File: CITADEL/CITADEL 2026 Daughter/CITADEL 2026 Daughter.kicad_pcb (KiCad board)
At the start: 2 copper layers, 35.8 x 35.5 mm, 4 parts, among them J1 Servo_Daughter

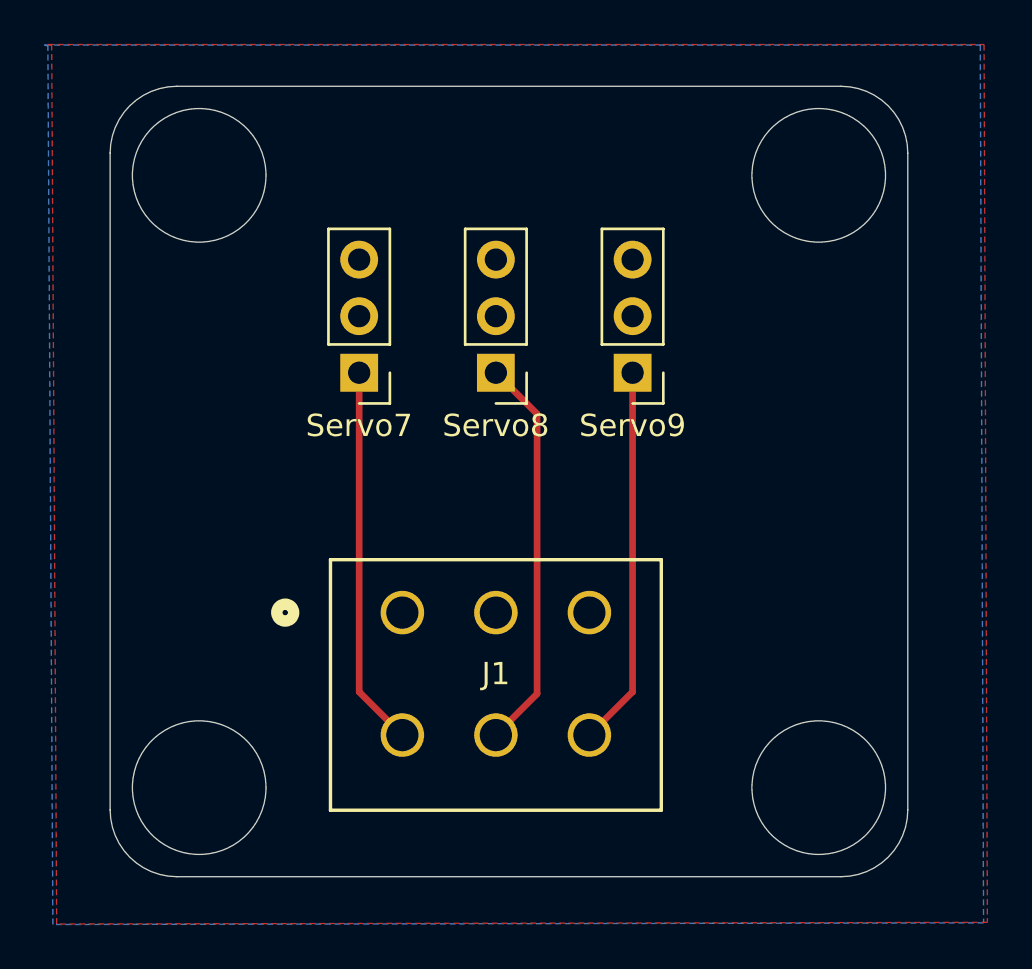
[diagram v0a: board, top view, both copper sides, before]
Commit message: Changed board to be square
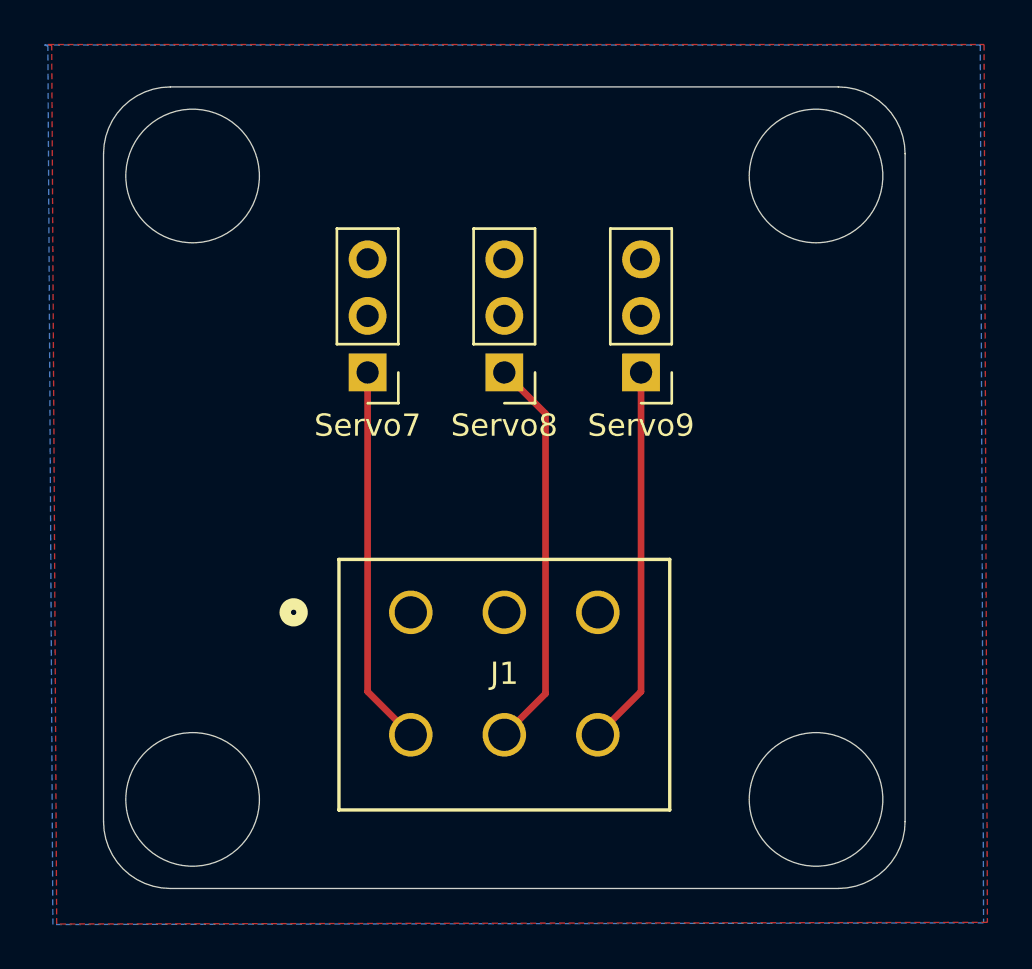
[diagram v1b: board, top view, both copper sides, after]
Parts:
- moved J1 0.38 mm to (39.1, 45.3)
- moved Servo7 0.38 mm to (37.1, 34.5)
- moved Servo8 0.38 mm to (43.3, 34.5)
- moved Servo9 0.38 mm to (49.4, 34.5)
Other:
- board size 35.8 x 35.5 mm -> 36 x 36 mm
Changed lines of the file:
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@@
 	(footprint "Connector_PinHeader_2.54mm:PinHeader_1x03_P2.54mm_Vertical"
 		(layer "F.Cu")
-		(at 36.76 34.49 180)
+		(at 37.13868 34.47748 180)
 		(descr "Through hole straight pin header, 1x03, 2.54mm pitch, single row")
 		(tags "Through hole pin header THT 1x03 2.54mm single row")
@@
 	(footprint "Jayse_Footprints:CONN_SD-5566-002_06_MOL"
 		(layer "F.Cu")
-		(at 38.700001 45.264001)
+		(at 39.078681 45.251481)
 		(tags "39281063 ")
 		(property "Reference" "J1"
@@
 	(footprint "Connector_PinHeader_2.54mm:PinHeader_1x03_P2.54mm_Vertical"
 		(layer "F.Cu")
-		(at 49.04 34.49 180)
+		(at 49.41868 34.47748 180)
 		(descr "Through hole straight pin header, 1x03, 2.54mm pitch, single row")
 		(tags "Through hole pin header THT 1x03 2.54mm single row")
@@
 	(footprint "Connector_PinHeader_2.54mm:PinHeader_1x03_P2.54mm_Vertical"
 		(layer "F.Cu")
-		(at 42.9 34.49 180)
+		(at 43.27868 34.47748 180)
 		(descr "Through hole straight pin header, 1x03, 2.54mm pitch, single row")
 		(tags "Through hole pin header THT 1x03 2.54mm single row")
@@
 	)
 	(gr_circle
-		(center 57.4 25.625)
-		(end 60.4 25.625)
+		(center 57.27868 25.65368)
+		(end 60.27868 25.65368)
 		(stroke
 			(width 0.05)
@@
 		(layer "Edge.Cuts")
 	)
+	(gr_arc
+		(start 28.27868 57.65368)
+		(mid 26.15736 56.775)
+		(end 25.27868 54.65368)
+		(stroke
+			(width 0.05)
+			(type default)
+		)
+		(layer "Edge.Cuts")
+	)
 	(gr_circle
-		(center 57.4 53.125)
-		(end 60.4 53.125)
+		(center 57.27868 53.65368)
+		(end 60.27868 53.65368)
 		(stroke
 			(width 0.05)
@@
 	)
 	(gr_arc
-		(start 58.4 21.625)
-		(mid 60.52132 22.50368)
-		(end 61.4 24.625)
+		(start 61.27868 54.65368)
+		(mid 60.4 56.775)
+		(end 58.27868 57.65368)
 		(stroke
 			(width 0.05)
@@
 		(layer "Edge.Cuts")
 	)
-	(gr_line
-		(start 58.4 57.125)
-		(end 28.575 57.125)
+	(gr_arc
+		(start 25.27868 24.65368)
+		(mid 26.15736 22.53236)
+		(end 28.27868 21.65368)
 		(stroke
 			(width 0.05)
@@
 	)
 	(gr_circle
-		(center 29.575 53.125)
-		(end 32.575 53.125)
+		(center 29.27868 53.65368)
+		(end 32.27868 53.65368)
 		(stroke
 			(width 0.05)
@@
 		(layer "Edge.Cuts")
 	)
-	(gr_arc
-		(start 28.575 57.125)
-		(mid 26.45368 56.24632)
-		(end 25.575 54.125)
+	(gr_line
+		(start 28.27868 21.65368)
+		(end 58.27868 21.65368)
 		(stroke
 			(width 0.05)
@@
 		(layer "Edge.Cuts")
 	)
-	(gr_arc
-		(start 61.4 54.125)
-		(mid 60.52132 56.24632)
-		(end 58.4 57.125)
+	(gr_line
+		(start 61.27868 24.65368)
+		(end 61.27868 54.65368)
 		(stroke
 			(width 0.05)
@@
 	)
 	(gr_circle
-		(center 29.575 25.625)
-		(end 32.575 25.625)
+		(center 29.27868 25.65368)
+		(end 32.27868 25.65368)
 		(stroke
 			(width 0.05)
@@
 	)
 	(gr_line
-		(start 25.575 54.125)
-		(end 25.575 24.625)
+		(start 58.27868 57.65368)
+		(end 28.27868 57.65368)
 		(stroke
 			(width 0.05)
@@
 	)
 	(gr_arc
-		(start 25.575 24.625)
-		(mid 26.45368 22.50368)
-		(end 28.575 21.625)
+		(start 58.27868 21.65368)
+		(mid 60.4 22.53236)
+		(end 61.27868 24.65368)
 		(stroke
 			(width 0.05)
@@
 	)
 	(gr_line
-		(start 61.4 24.625)
-		(end 61.4 54.125)
+		(start 25.27868 54.65368)
+		(end 25.27868 24.65368)
 		(stroke
 			(width 0.05)
@@
 		(layer "Edge.Cuts")
 	)
-	(gr_line
-		(start 28.575 21.625)
-		(end 58.4 21.625)
-		(stroke
-			(width 0.05)
-			(type default)
-		)
-		(layer "Edge.Cuts")
+	(dimension
+		(type orthogonal)
+		(layer "Cmts.User")
+		(pts
+			(xy 57.27868 25.65368) (xy 57.27868 53.65368)
+		)
+		(height 12.74632)
+		(orientation 1)
+		(format
+			(prefix "")
+			(suffix "")
+			(units 3)
+			(units_format 0)
+			(precision 4)
+			(suppress_zeroes yes)
+		)
+		(style
+			(thickness 0.1)
+			(arrow_length 1.27)
+			(text_position_mode 0)
+			(arrow_direction outward)
+			(extension_height 0.58642)
+			(extension_offset 0.5)
+			(keep_text_aligned yes)
+		)
+		(gr_text "28"
+			(at 68.875 39.65368 90)
+			(layer "Cmts.User")
+			(effects
+				(font
+					(size 1 1)
+					(thickness 0.15)
+				)
+			)
+		)
+	)
+	(dimension
+		(type orthogonal)
+		(layer "Cmts.User")
+		(pts
+			(xy 57.27868 25.65368) (xy 29.27868 25.65368)
+		)
+		(height -9.20368)
+		(orientation 0)
+		(format
+			(prefix "")
+			(suffix "")
+			(units 3)
+			(units_format 0)
+			(precision 4)
+			(suppress_zeroes yes)
+		)
+		(style
+			(thickness 0.1)
+			(arrow_length 1.27)
+			(text_position_mode 0)
+			(arrow_direction outward)
+			(extension_height 0.58642)
+			(extension_offset 0.5)
+			(keep_text_aligned yes)
+		)
+		(gr_text "28"
+			(at 43.27868 15.3 0)
+			(layer "Cmts.User")
+			(effects
+				(font
+					(size 1 1)
+					(thickness 0.15)
+				)
+			)
+		)
 	)
 	(segment
-		(start 38.700001 50.764)
-		(end 36.76 48.823999)
+		(start 39.078681 50.75148)
+		(end 37.13868 48.811479)
 		(width 0.3)
 		(layer "F.Cu")
@@
 	)
 	(segment
-		(start 36.76 48.823999)
-		(end 36.76 34.49)
+		(start 37.13868 48.811479)
+		(end 37.13868 34.47748)
 		(width 0.3)
 		(layer "F.Cu")
@@
 	)
 	(segment
-		(start 49.04 48.823999)
-		(end 49.04 34.49)
+		(start 49.41868 48.811479)
+		(end 49.41868 34.47748)
 		(width 0.3)
 		(layer "F.Cu")
@@
 	)
 	(segment
-		(start 47.099999 50.764)
-		(end 49.04 48.823999)
+		(start 47.478679 50.75148)
+		(end 49.41868 48.811479)
 		(width 0.3)
 		(layer "F.Cu")
@@
 	)
 	(segment
-		(start 42.9 50.764)
-		(end 44.75 48.914)
+		(start 43.27868 50.75148)
+		(end 45.12868 48.90148)
 		(width 0.3)
 		(layer "F.Cu")
@@
 	)
 	(segment
-		(start 44.75 36.34)
-		(end 42.9 34.49)
+		(start 45.12868 36.32748)
+		(end 43.27868 34.47748)
 		(width 0.3)
 		(layer "F.Cu")
@@
 	)
 	(segment
-		(start 44.75 48.914)
-		(end 44.75 36.34)
+		(start 45.12868 48.90148)
+		(end 45.12868 36.32748)
 		(width 0.3)
 		(layer "F.Cu")

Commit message: Updated servo connectors
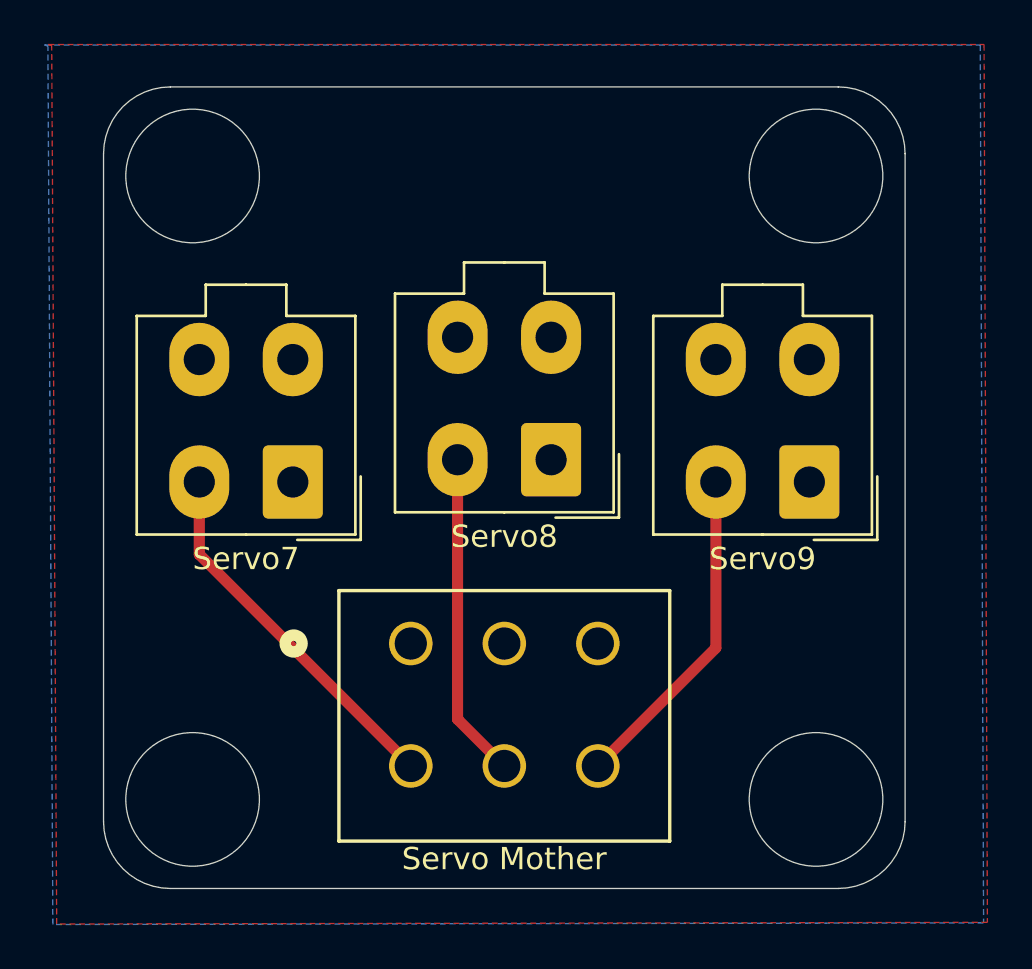
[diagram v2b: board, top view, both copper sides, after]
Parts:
- Servo Mother: renamed from J1
- Servo7, Servo8, Servo9: footprint Connector_PinHeader_2.54mm:PinHeader_1x03_P2.54mm_Vertical -> Connector_Molex:Molex_Mini-Fit_Jr_5566-04A_2x02_P4.20mm_Vertical
- moved Servo9 9.02 mm to (57.0, 39.4)
- moved Servo7 5.96 mm to (33.8, 39.4)
- moved Servo8 4.45 mm to (45.4, 38.4)
- moved Servo Mother 1.40 mm to (39.1, 46.7)
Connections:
- Servo7 pad 1: /Servo7 -> GND
- Servo7 pad 2: +5V -> /Servo7
- Servo7 pad 3: GND -> +5V
- Servo8 pad 1: /Servo8 -> GND
- Servo8 pad 2: +5V -> /Servo8
- Servo8 pad 3: GND -> +5V
- Servo9 pad 1: /Servo9 -> GND
- Servo9 pad 2: +5V -> /Servo9
- Servo9 pad 3: GND -> +5V
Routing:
- net /Servo8: track 17.8 -> 14.6 mm
- net /Servo9: track 17.1 -> 14.9 mm

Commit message: Changed back plane to GND and added 5V zone
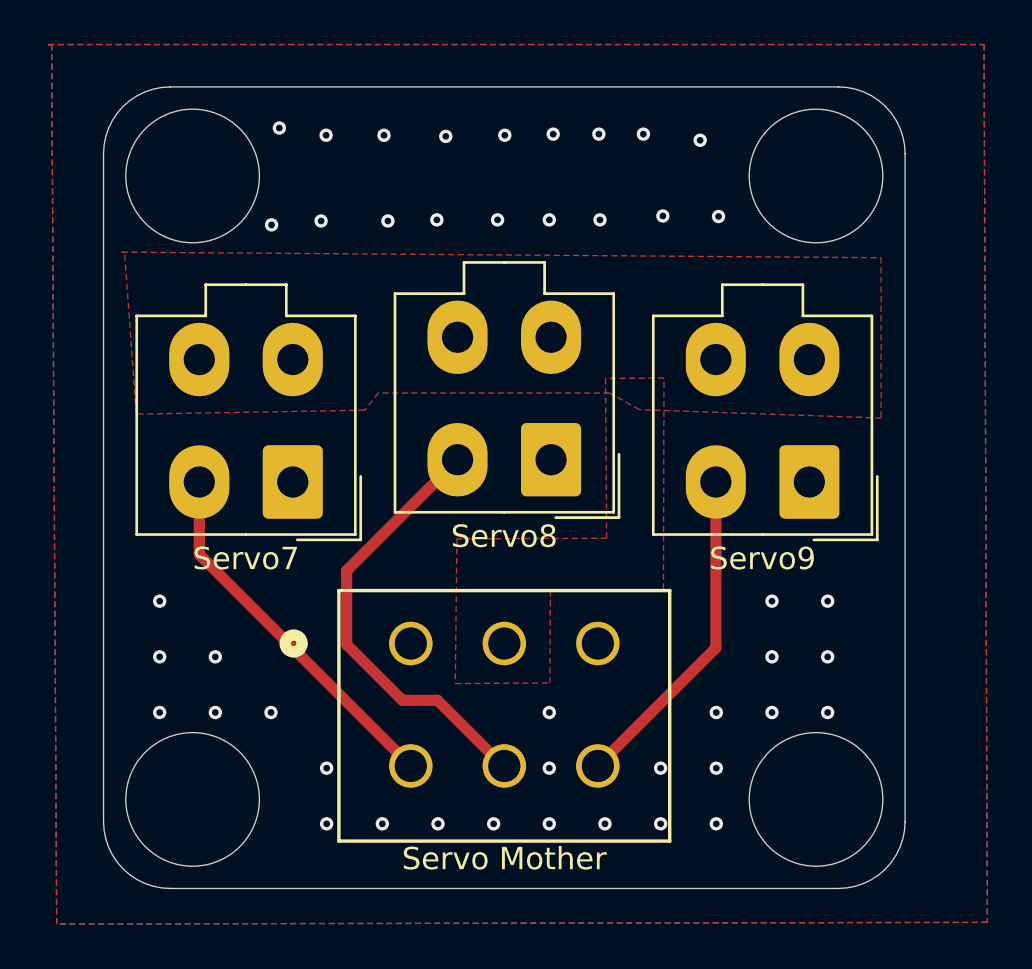
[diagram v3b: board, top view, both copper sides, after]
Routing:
- net /Servo8: track 14.6 -> 19.7 mm
- net GND: vias 0 -> 44
- added copper zone on F.Cu, net +5V
- added copper zone on B.Cu, net GND
- removed copper zone on B.Cu, net +5V
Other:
- board text added: "{ "ViaStitching": "0.2", "stitch_zone_0": { "HSpacing": "2.5", "VSpacing": "2.5", "HOffset": "0", "VOffset": "0", "Clearance": "0.6", "Randomize": false } }"
